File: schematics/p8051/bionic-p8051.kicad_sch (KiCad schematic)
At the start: 6 parts, among them J1 Bionic-P135, J2 Bionic-P245, U1 P8051AH, U2 74HCT126, U3 11AA010-I/TO

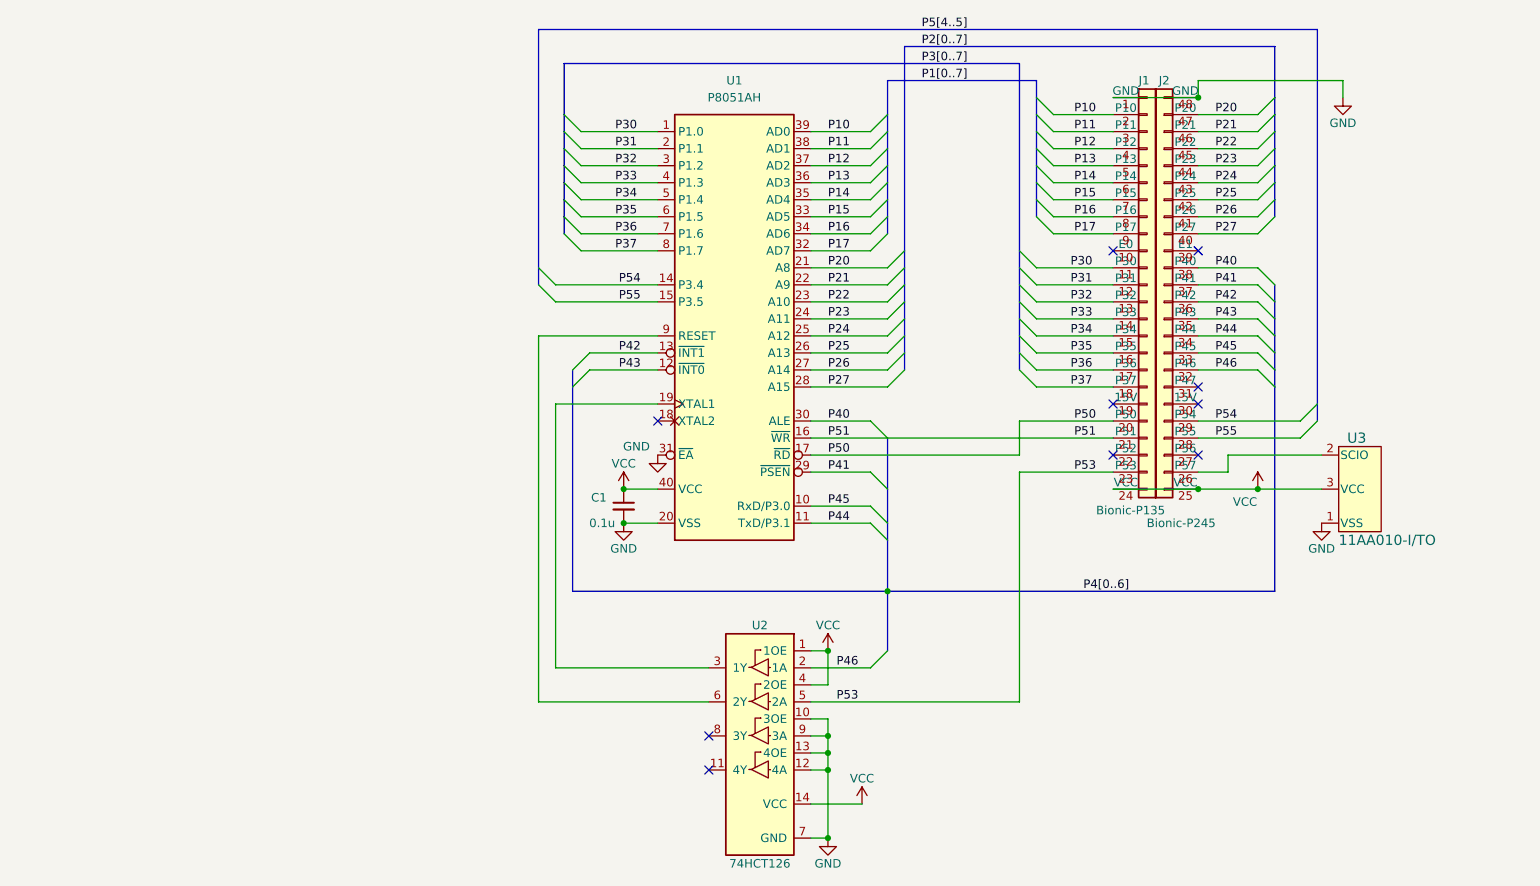
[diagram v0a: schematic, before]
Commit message: [P8051] Support P8051
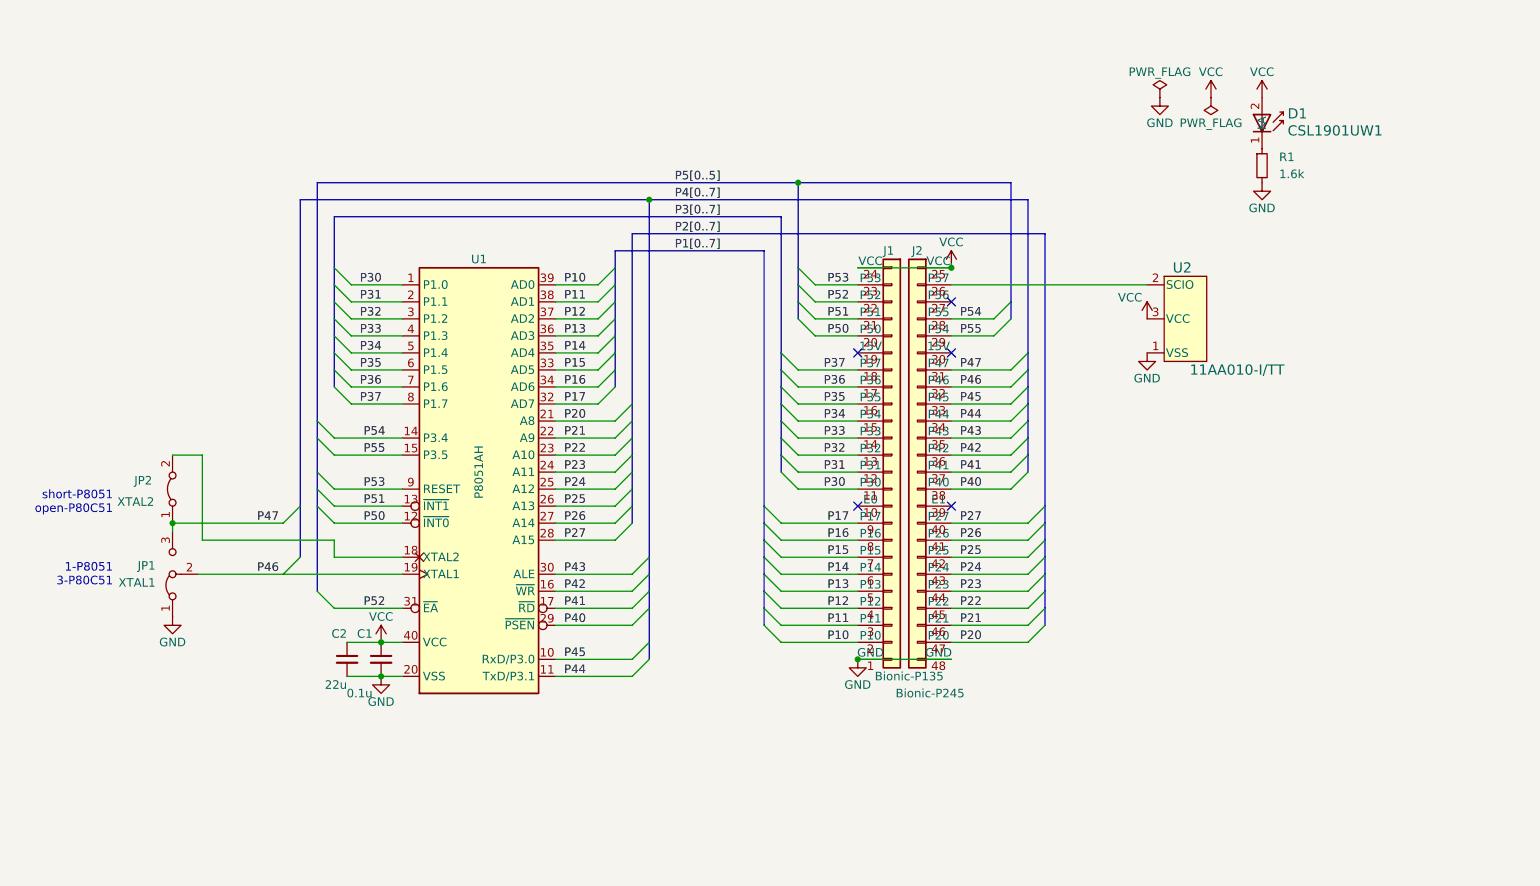
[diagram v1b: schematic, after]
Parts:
- removed U2: 74HCT126, Package_DIP:DIP-14_W7.62mm, symbol 0-LocalLibrary:74HCT126
- removed U3: 11AA010-I/TO, TO-92_MC_MCH, symbol 0-LocalLibrary:11AA010-I_TO
- added C2: 22u, Resistor_SMD:R_0603_1608Metric_Pad0.98x0.95mm_HandSolder, symbol Device:C_Small
- added D1: CSL1901UW1, 0-LocalLibrary:LED_CSL1901UW1_ROM, symbol 0-LocalLibrary:CSL1901UW1
- added JP1: XTAL1, 0-LocalLibrary:SolderJumper-3_P1.3mm_Open_RoundedPad1.0x1.5mm_NumberLabels, symbol Jumper:Jumper_3_Bridged12
- added JP2: XTAL2, 0-LocalLibrary:SolderJumper-2_P1.3mm_Open_RoundedPad1.0x1.5mm, symbol Jumper:Jumper_2_Bridged
- added R1: 1.6k, Resistor_SMD:R_0603_1608Metric_Pad0.98x0.95mm_HandSolder, symbol Device:R_Small
- added U2: 11AA010-I/TT, 0-LocalLibrary:SOT-23_MC_MCH-M, symbol 0-LocalLibrary:11AA010-I_TT
- C1: footprint Capacitor_THT:C_Disc_D3.4mm_W2.1mm_P2.50mm -> Resistor_SMD:R_0603_1608Metric_Pad0.98x0.95mm_HandSolder
- U1: footprint Package_DIP:DIP-40_W15.24mm -> 0-LocalLibrary:DIP-40_W15.24mm_Socket
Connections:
- net GND: now also C2.2, JP1.1 (A), R1.2, U2.1 (VSS); no longer U1.31 (~{EA})
- net P40: now also U1.29 (~{PSEN}); no longer U1.30 (ALE)
- net P41: now also U1.17 (~{RD}); no longer U1.29 (~{PSEN})
- net P42: now also U1.16 (~{WR}); no longer U1.13 (~{INT1})
- net P43: now also U1.30 (ALE); no longer U1.12 (~{INT0})
- net P46: now also U1.19 (XTAL1), JP1.2 (C)
- net P50: now also U1.12 (~{INT0}); no longer U1.17 (~{RD})
- net P51: now also U1.13 (~{INT1}); no longer U1.16 (~{WR})
- net P53: now also U1.9 (RESET)
- net P54: now also J2.28 (P55); no longer J2.29 (P54)
- net P55: now also J2.29 (P54); no longer J2.28 (P55)
- net VCC: now also C2.1, D1.2 (A), U2.3 (VCC)
- net P52: now reaches J1.22 (P52)
- net P52: now also U1.31 (~{EA})
- net at U1.18 (XTAL2): now also JP2.2 (B)
- net at J2.26 (P57): now also U2.2 (SCIO)
- net P47: now reaches J2.31 (P47)
- net P47: now also JP1.3 (B), JP2.1 (A)
- new net: D1.1 (K), R1.1
- no-connect marks 10 -> 5
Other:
- note added: "1-P8051 3-P80C51"
- note added: "short-P8051 open-P80C51"
- moved on the sheet: C1

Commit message: [P8051] Fix EEPROM pinout
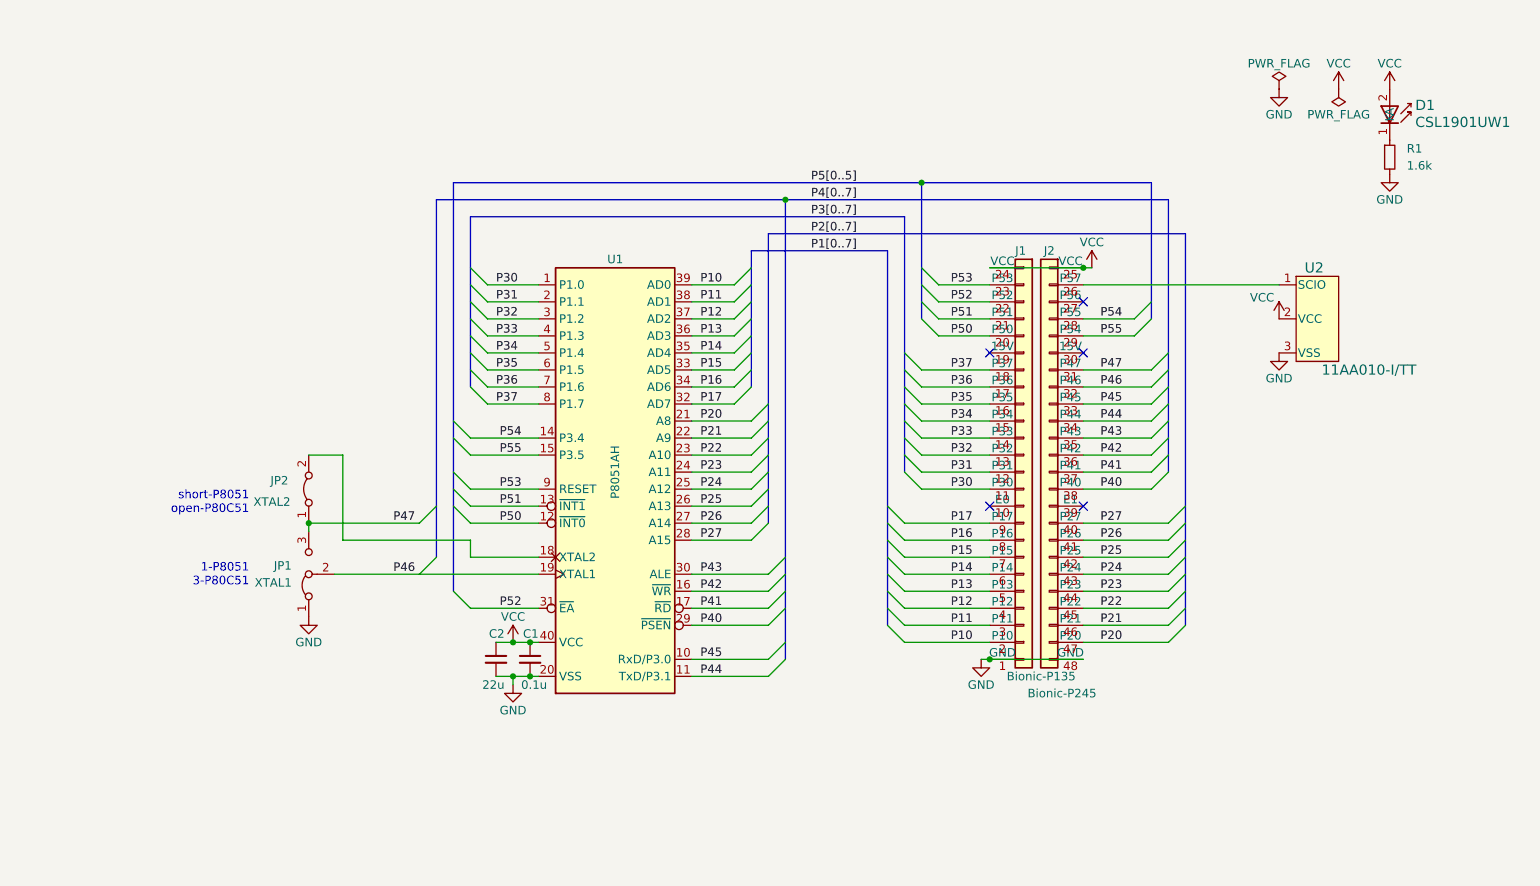
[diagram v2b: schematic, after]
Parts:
- J1: footprint connector:Bionic-P135_Vertical -> 0-LocalLibrary:Bionic-P135_Vertical
- J2: footprint connector:Bionic-P245_Vertical -> 0-LocalLibrary:Bionic-P245_Vertical
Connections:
- net GND: now also U2.3 (VSS); no longer U2.1 (VSS)
- net VCC: now also U2.2 (VCC); no longer U2.3 (VCC)
- net at J2.26 (P57): now also U2.1 (SCIO); no longer U2.2 (SCIO)
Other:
- moved on the sheet: C1, C2, D1, J1, J2, JP1, JP2, R1, U1, U2

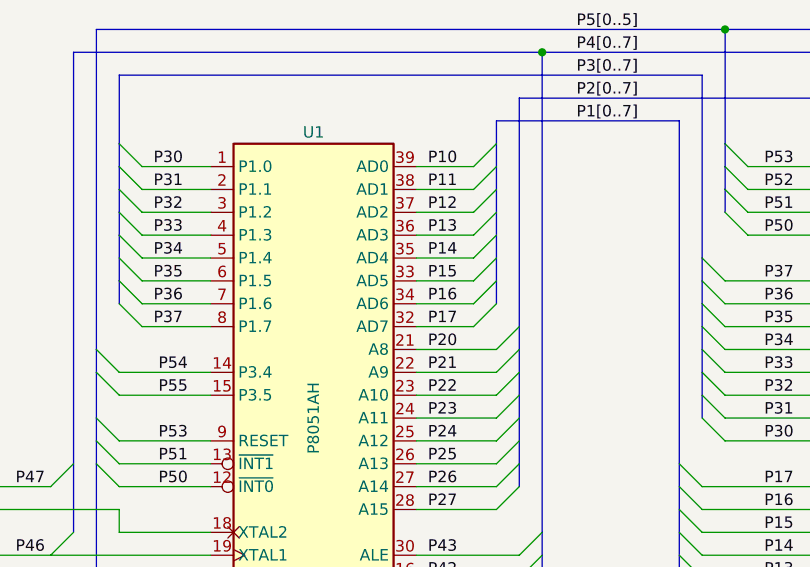
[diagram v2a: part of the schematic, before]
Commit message: [P8051] Fix P8051 footprint
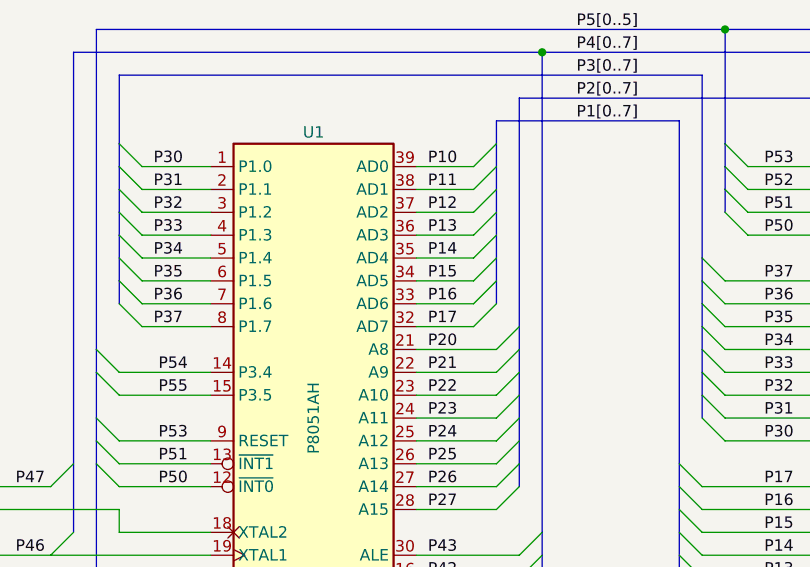
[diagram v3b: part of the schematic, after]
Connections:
- net P15: now also U1.34 (AD5); no longer U1.33 (AD5)
- net P16: now also U1.33 (AD6); no longer U1.34 (AD6)
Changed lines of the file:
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@@
   (title_block
     (title "BionicP8051")
-    (date "2024-11-01")
-    (rev "4")
+    (date "2024-12-02")
+    (rev "5")
     (company "Tadashi G. Takaoka")
   )

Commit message: [schematics] Update LED footprint
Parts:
- D1: footprint 0-LocalLibrary:LED_CSL1901UW1_ROM -> 0-LocalLibrary:LED_CSL1901UW1_ROM-M

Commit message: [P8051] Cleanup schematics
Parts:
- D1: footprint 0-LocalLibrary:LED_CSL1901UW1_ROM-M -> rhom:LED_CSL1901UW1_ROM-M; symbol 0-LocalLibrary:CSL1901UW1 -> rhom:CSL1901UW1
- J1: footprint 0-LocalLibrary:Bionic-P135_Vertical -> bionic:Bionic-P135_Vertical; symbol 0-LocalLibrary:Bionic-P135 -> bionic:Bionic-P135
- J2: footprint 0-LocalLibrary:Bionic-P245_Vertical -> bionic:Bionic-P245_Vertical; symbol 0-LocalLibrary:Bionic-P245 -> bionic:Bionic-P245
- JP1: footprint 0-LocalLibrary:SolderJumper-3_P1.3mm_Open_RoundedPad1.0x1.5mm_NumberLabels -> bionic:SolderJumper-3_P1.3mm_Open_RoundedPad1.0x1.5mm_NumberLabels
- JP2: footprint 0-LocalLibrary:SolderJumper-2_P1.3mm_Open_RoundedPad1.0x1.5mm -> bionic:SolderJumper-2_P1.3mm_Open_RoundedPad1.0x1.5mm
- U1: footprint 0-LocalLibrary:DIP-40_W15.24mm_Socket -> bionic:DIP-40_W15.24mm_Socket; symbol 0-LocalLibrary:P8051AH -> cpu:P8051AH
- U2: footprint 0-LocalLibrary:SOT-23_MC_MCH-M -> microchip:SOT-23_MC_MCH-M; symbol 0-LocalLibrary:11AA010-I_TT -> microchip:11AA010-I_TT
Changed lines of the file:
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@@
 			)
 		)
-		(property "Footprint" "0-LocalLibrary:SolderJumper-2_P1.3mm_Open_RoundedPad1.0x1.5mm"
+		(property "Footprint" "bionic:SolderJumper-2_P1.3mm_Open_RoundedPad1.0x1.5mm"
 			(at 64.77 104.14 0)
 			(effects
@@
 	)
 	(symbol
-		(lib_id "0-LocalLibrary:Bionic-P245")
+		(lib_id "bionic:Bionic-P245")
 		(at 179.07 99.06 0)
 		(unit 1)
@@
 			)
 		)
-		(property "Footprint" "0-LocalLibrary:Bionic-P245_Vertical"
+		(property "Footprint" "bionic:Bionic-P245_Vertical"
 			(at 180.34 134.62 0)
 			(effects
@@
 			)
 		)
-		(property "Description" ""
+		(property "Description" "Generic connector, single row, 01x24, script generated (kicad-library-utils/schlib/autogen/connector/)"
 			(at 179.07 99.06 0)
 			(effects
@@
 	)
 	(symbol
-		(lib_id "0-LocalLibrary:Bionic-P135")
+		(lib_id "bionic:Bionic-P135")
 		(at 171.45 99.06 0)
 		(unit 1)
@@
 			)
 		)
-		(property "Footprint" "0-LocalLibrary:Bionic-P135_Vertical"
+		(property "Footprint" "bionic:Bionic-P135_Vertical"
 			(at 172.72 134.62 0)
 			(effects
@@
 			)
 		)
-		(property "Description" ""
+		(property "Description" "Generic connector, single row, 01x24, script generated (kicad-library-utils/schlib/autogen/connector/)"
 			(at 171.45 99.06 0)
 			(effects
@@
 			)
 		)
-		(property "Footprint" "0-LocalLibrary:SolderJumper-3_P1.3mm_Open_RoundedPad1.0x1.5mm_NumberLabels"
+		(property "Footprint" "bionic:SolderJumper-3_P1.3mm_Open_RoundedPad1.0x1.5mm_NumberLabels"
 			(at 64.77 116.84 0)
 			(effects
@@
 	)
 	(symbol
-		(lib_id "0-LocalLibrary:CSL1901UW1")
+		(lib_id "rhom:CSL1901UW1")
 		(at 226.06 44.45 270)
 		(unit 1)
@@
 		(fields_autoplaced yes)
 		(property "Reference" "D1"
-			(at 229.87 46.863 90)
+			(at 229.87 46.8629 90)
 			(effects
 				(font
@@
 		)
 		(property "Value" "CSL1901UW1"
-			(at 229.87 49.403 90)
+			(at 229.87 49.4029 90)
 			(effects
 				(font
@@
 			)
 		)
-		(property "Footprint" "0-LocalLibrary:LED_CSL1901UW1_ROM-M"
+		(property "Footprint" "rhom:LED_CSL1901UW1_ROM-M"
 			(at 217.17 48.26 0)
 			(effects
@@
 	)
 	(symbol
-		(lib_id "0-LocalLibrary:11AA010-I_TT")
+		(lib_id "microchip:11AA010-I_TT")
 		(at 212.09 72.39 0)
 		(unit 1)
@@
 			)
 		)
-		(property "Footprint" "0-LocalLibrary:SOT-23_MC_MCH-M"
+		(property "Footprint" "microchip:SOT-23_MC_MCH-M"
 			(at 214.63 90.17 0)
 			(effects
@@
 			)
 		)
-		(property "Description" ""
+		(property "Description" "UNI/O Serial EEPROM (1Kbit)"
 			(at 212.09 72.39 0)
 			(effects
@@
 	)
 	(symbol
-		(lib_id "0-LocalLibrary:P8051AH")
+		(lib_id "cpu:P8051AH")
 		(at 110.49 101.6 0)
 		(unit 1)
@@
 			)
 		)
-		(property "Footprint" "0-LocalLibrary:DIP-40_W15.24mm_Socket"
+		(property "Footprint" "bionic:DIP-40_W15.24mm_Socket"
 			(at 111.76 135.89 0)
 			(effects
@@
 			)
 		)
-		(property "Description" ""
+		(property "Description" "8-bit General Purpose Microprocessor, DIP-40"
 			(at 110.49 101.6 0)
 			(effects

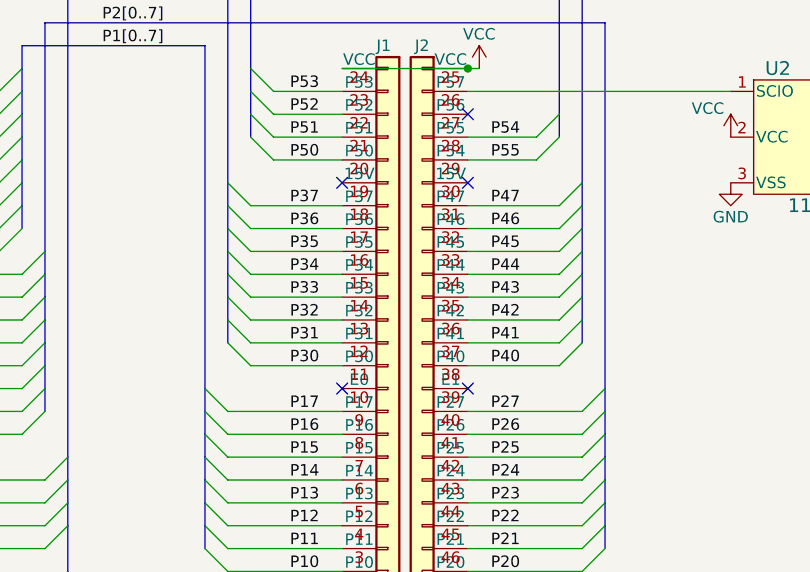
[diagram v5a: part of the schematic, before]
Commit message: [P8051] Update schematics
Remove unused pins from bionic connector
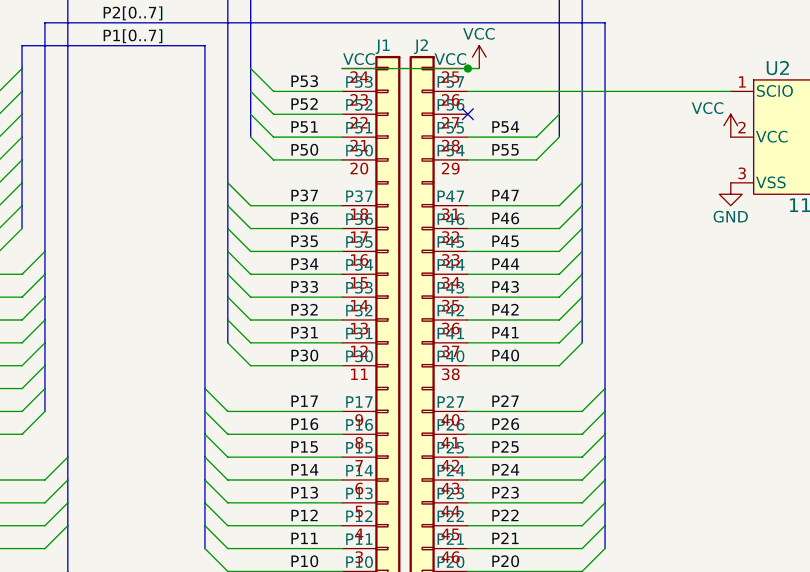
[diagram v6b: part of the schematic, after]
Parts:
- J1: footprint bionic:Bionic-P135_Vertical -> bionic:Bionic-P135_THT
- J2: footprint bionic:Bionic-P245_Vertical -> bionic:Bionic-P245_THT
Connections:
- no-connect marks 5 -> 1
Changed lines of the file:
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@@
 	(title_block
 		(title "BionicP8051")
-		(date "2024-12-02")
-		(rev "5")
+		(date "2025-03-02")
+		(rev "6")
 		(company "Tadashi G. Takaoka")
 	)
@@
 	)
 	(no_connect
-		(at 180.34 106.68)
-	)
-	(no_connect
-		(at 166.37 83.82)
-	)
-	(no_connect
-		(at 166.37 106.68)
-	)
-	(no_connect
 		(at 180.34 76.2)
 	)
-	(no_connect
-		(at 180.34 83.82)
-	)
 	(bus_entry
 		(at 153.67 99.06)
@@
 			)
 		)
-		(property "Footprint" "bionic:Bionic-P245_Vertical"
+		(property "Footprint" "bionic:Bionic-P245_THT"
 			(at 180.34 134.62 0)
 			(effects
@@
 		(pin "48"
 		)
-		(pin "39"
-		)
 		(pin "42"
 		)
@@
 		(pin "36"
 		)
-		(pin "30"
-		)
 		(pin "47"
 		)
@@
 			)
 		)
-		(property "Footprint" "bionic:Bionic-P135_Vertical"
+		(property "Footprint" "bionic:Bionic-P135_THT"
 			(at 172.72 134.62 0)
 			(effects
@@
 		(pin "23"
 		)
-		(pin "19"
-		)
-		(pin "10"
-		)
 		(pin "13"
